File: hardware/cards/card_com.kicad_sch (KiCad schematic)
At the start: 18 parts, among them J1 DE9_Pins, J2 Conn_01x03, J3 Conn_01x04, U1 16550, U2 MAX3241, U3 74HCT04, U4 74HCT08, U5 74HCT08, U6 74HCT125

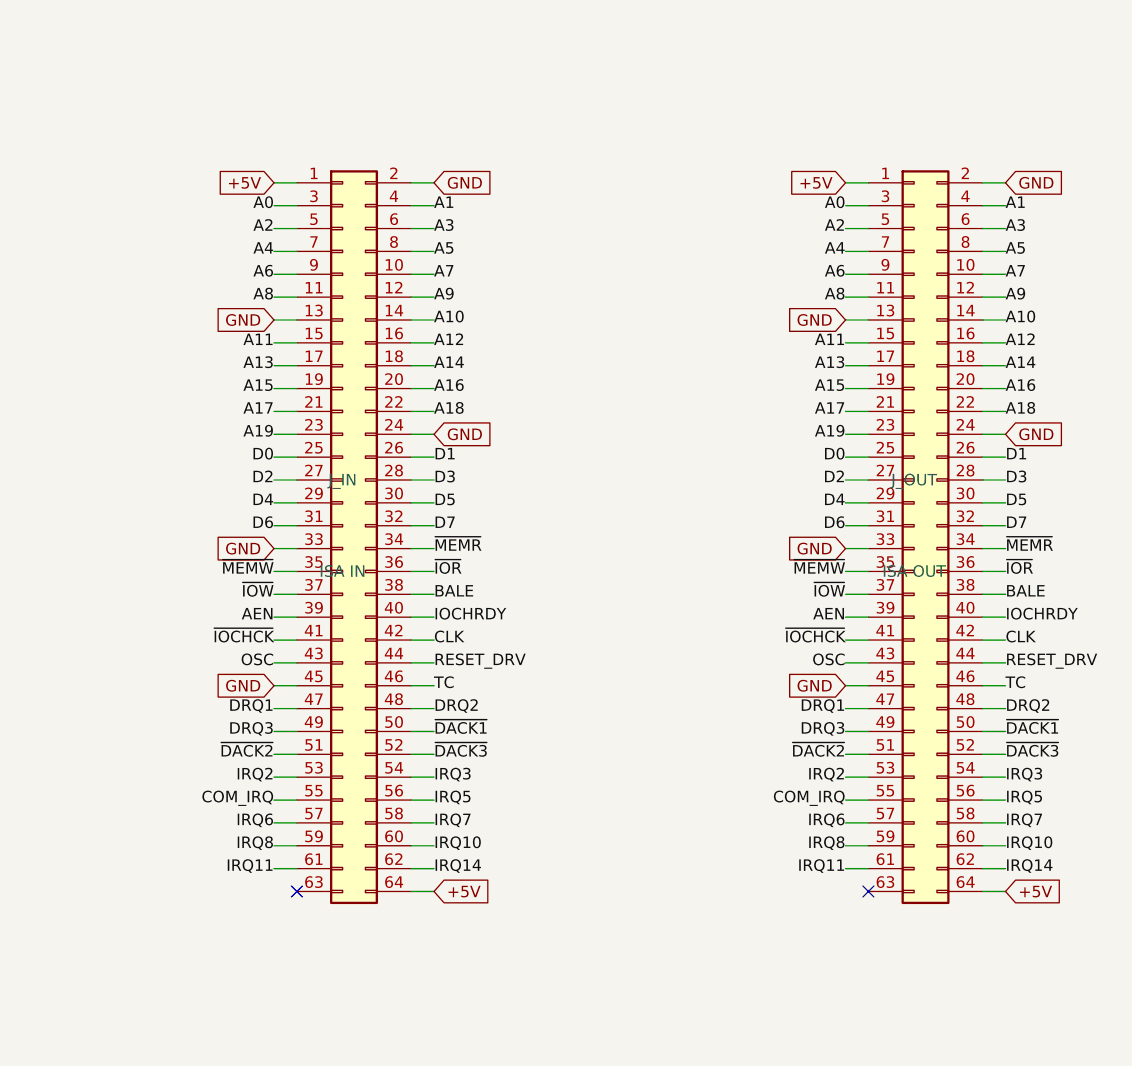
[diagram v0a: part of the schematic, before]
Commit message: Re-base ISA connector on standard 8-bit ISA pinout (60-pin, PicoGUS-style)
isa_conn now uses the standard 8-bit ISA edge pinout on a 60-pin 2.54mm header
(Conn_02x30_Odd_Even), matching the PicoGUS Bus_ISA_8bit layout so the sidecar and
dev cards are pin-compatible with real ISA cards (and 60-pin ribbon is easy to
source). The unused ISA analog rails are reclaimed: pin7 -5V->~{IOCHCK}, pin11
-12V->GND (extra return), pin15 +12V->IRQ8; pin13 reserved/0WS# left NC. Drops the
non-standard IRQ10/11/14 (16-bit-extension signals on a real AT); DACK0/REFRESH#
now on its standard pin (undriven, for card compatibility). Change is confined to
isa_conn.py; sidecar + all card_* sheets inherit it. Verified pin map and
connectivity (IOCHCK->Bus MCU, IRQ8->collector+RTC); zero structural ERC on
motherboard and all five cards.

Co-Authored-By: Claude Opus 4.8 (1M context) <noreply@anthropic.com>
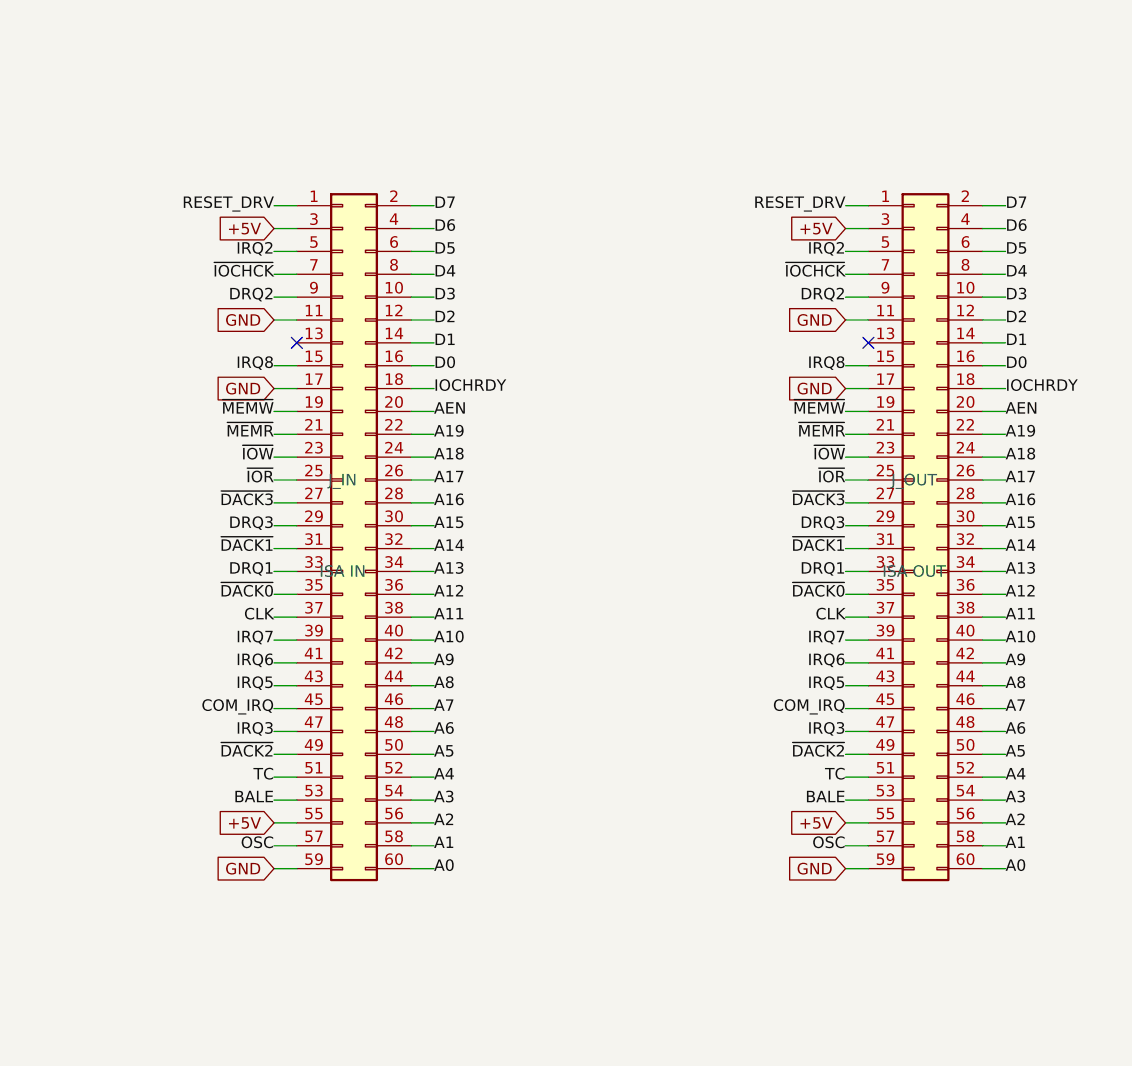
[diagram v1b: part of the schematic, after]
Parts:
- removed J_IN: ISA IN, symbol Connector_Generic:Conn_02x32_Odd_Even
- removed J_OUT: ISA OUT, symbol Connector_Generic:Conn_02x32_Odd_Even
- added J_IN: ISA IN, symbol Connector_Generic:Conn_02x30_Odd_Even
- added J_OUT: ISA OUT, symbol Connector_Generic:Conn_02x30_Odd_Even
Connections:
- net +5V: now also J_IN.3 (Pin_3), J_IN.55 (Pin_55), J_OUT.3 (Pin_3), J_OUT.55 (Pin_55)
- net A0: now also J_IN.60 (Pin_60), J_OUT.60 (Pin_60)
- net A1: now also J_IN.58 (Pin_58), J_OUT.58 (Pin_58)
- net A10: now also J_IN.40 (Pin_40), J_OUT.40 (Pin_40)
- net A11: now also J_IN.38 (Pin_38), J_OUT.38 (Pin_38)
- net A12: now also J_IN.36 (Pin_36), J_OUT.36 (Pin_36)
- net A13: now also J_IN.34 (Pin_34), J_OUT.34 (Pin_34)
- net A14: now also J_IN.32 (Pin_32), J_OUT.32 (Pin_32)
- net A15: now also J_IN.30 (Pin_30), J_OUT.30 (Pin_30)
- net A16: now also J_IN.28 (Pin_28), J_OUT.28 (Pin_28)
- net A17: now also J_IN.26 (Pin_26), J_OUT.26 (Pin_26)
- net A18: now also J_IN.24 (Pin_24), J_OUT.24 (Pin_24)
- net A19: now also J_IN.22 (Pin_22), J_OUT.22 (Pin_22)
- net A2: now also J_IN.56 (Pin_56), J_OUT.56 (Pin_56)
- net A3: now also J_IN.54 (Pin_54), J_OUT.54 (Pin_54)
- net A4: now also J_IN.52 (Pin_52), J_OUT.52 (Pin_52)
- net A5: now also J_IN.50 (Pin_50), J_OUT.50 (Pin_50)
- net A6: now also J_IN.48 (Pin_48), J_OUT.48 (Pin_48)
- net A7: now also J_IN.46 (Pin_46), J_OUT.46 (Pin_46)
- net A8: now also J_IN.44 (Pin_44), J_OUT.44 (Pin_44)
- net A9: now also J_IN.42 (Pin_42), J_OUT.42 (Pin_42)
- net AEN: now also J_IN.20 (Pin_20), J_OUT.20 (Pin_20)
- net BALE: now also J_IN.53 (Pin_53), J_OUT.53 (Pin_53)
- net CLK: now also J_IN.37 (Pin_37), J_OUT.37 (Pin_37)
- net COM_IRQ: now also J_IN.45 (Pin_45), J_OUT.45 (Pin_45)
- net D0: now also J_IN.16 (Pin_16), J_OUT.16 (Pin_16)
- net D1: now also J_IN.14 (Pin_14), J_OUT.14 (Pin_14)
- net D2: now also J_IN.12 (Pin_12), J_OUT.12 (Pin_12)
- net D3: now also J_IN.10 (Pin_10), J_OUT.10 (Pin_10)
- net D4: now also J_IN.8 (Pin_8), J_OUT.8 (Pin_8)
- net D5: now also J_IN.6 (Pin_6), J_OUT.6 (Pin_6)
- net D6: now also J_IN.4 (Pin_4), J_OUT.4 (Pin_4)
- net D7: now also J_IN.2 (Pin_2), J_OUT.2 (Pin_2)
- net DRQ1: now also J_IN.33 (Pin_33), J_OUT.33 (Pin_33)
- net DRQ2: now also J_IN.9 (Pin_9), J_OUT.9 (Pin_9)
- net DRQ3: now also J_IN.29 (Pin_29), J_OUT.29 (Pin_29)
- net GND: now also J_IN.11 (Pin_11), J_IN.17 (Pin_17), J_IN.59 (Pin_59), J_OUT.11 (Pin_11), J_OUT.17 (Pin_17), J_OUT.59 (Pin_59)
- net IOCHRDY: now also J_IN.18 (Pin_18), J_OUT.18 (Pin_18)
- net IRQ2: now also J_IN.5 (Pin_5), J_OUT.5 (Pin_5)
- net IRQ3: now also J_IN.47 (Pin_47), J_OUT.47 (Pin_47)
- net IRQ5: now also J_IN.43 (Pin_43), J_OUT.43 (Pin_43)
- net IRQ6: now also J_IN.41 (Pin_41), J_OUT.41 (Pin_41)
- net IRQ7: now also J_IN.39 (Pin_39), J_OUT.39 (Pin_39)
- net IRQ8: now also J_IN.15 (Pin_15), J_OUT.15 (Pin_15)
- net OSC: now also J_IN.57 (Pin_57), J_OUT.57 (Pin_57)
- net RESET_DRV: now also J_IN.1 (Pin_1), J_OUT.1 (Pin_1)
- net TC: now also J_IN.51 (Pin_51), J_OUT.51 (Pin_51)
- net ~{DACK1}: now also J_IN.31 (Pin_31), J_OUT.31 (Pin_31)
- net ~{DACK2}: now also J_IN.49 (Pin_49), J_OUT.49 (Pin_49)
- net ~{DACK3}: now also J_IN.27 (Pin_27), J_OUT.27 (Pin_27)
- net ~{IOCHCK}: now also J_IN.7 (Pin_7), J_OUT.7 (Pin_7)
- net ~{IOR}: now also J_IN.25 (Pin_25), J_OUT.25 (Pin_25)
- net ~{IOW}: now also J_IN.23 (Pin_23), J_OUT.23 (Pin_23)
- net ~{MEMR}: now also J_IN.21 (Pin_21), J_OUT.21 (Pin_21)
- net ~{MEMW}: now also J_IN.19 (Pin_19), J_OUT.19 (Pin_19)
- new net ~{DACK0}: J_IN.35 (Pin_35), J_OUT.35 (Pin_35)

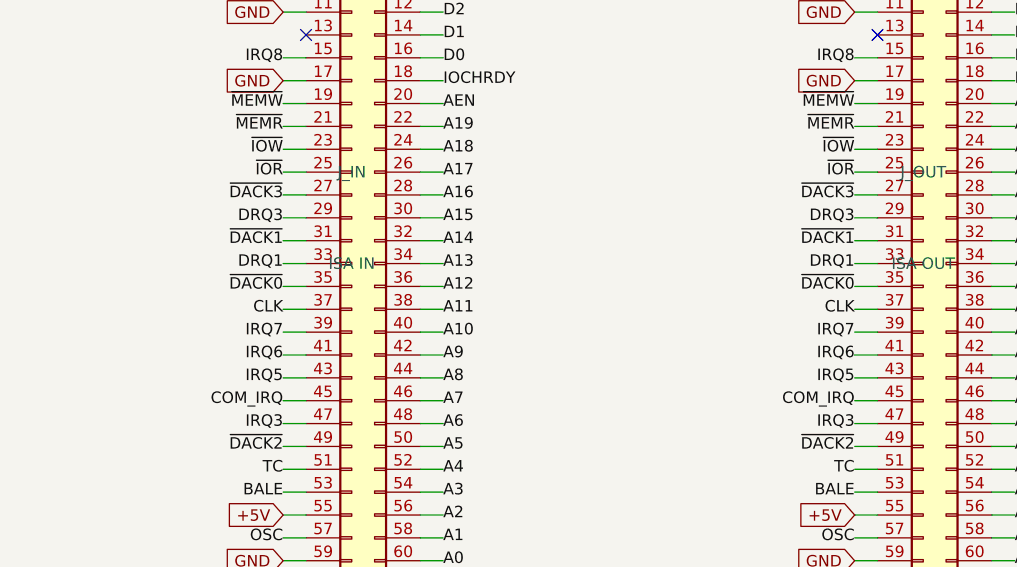
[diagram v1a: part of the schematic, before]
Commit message: Drive ISA REFRESH# from the Bus MCU for DRAM-based cards
Pin 35 (DACK0/REFRESH#) net renamed ~{DACK0} -> ~{REFRESH} in isa_conn and is now
an active Bus MCU output (GPIO47, reclaimed from the redundant raw-~WR sense -- the
MCU tracks writes via the gated MEMW/IOW). Driven from the internal ~15us refresh
timer (same source as the 0x61-bit-4 toggle); a refresh cycle reuses the bus-master
engine to walk the row address on A0-A7 + pulse MEMR#, so DRAM ISA cards see a
standard refresh. ~{REFRESH} added to the Bus MCU interface. Verified it ties
sidecar<->Bus MCU and passes through J_IN<->J_OUT on every dev card; zero
structural ERC on motherboard and all five cards.

Co-Authored-By: Claude Opus 4.8 (1M context) <noreply@anthropic.com>
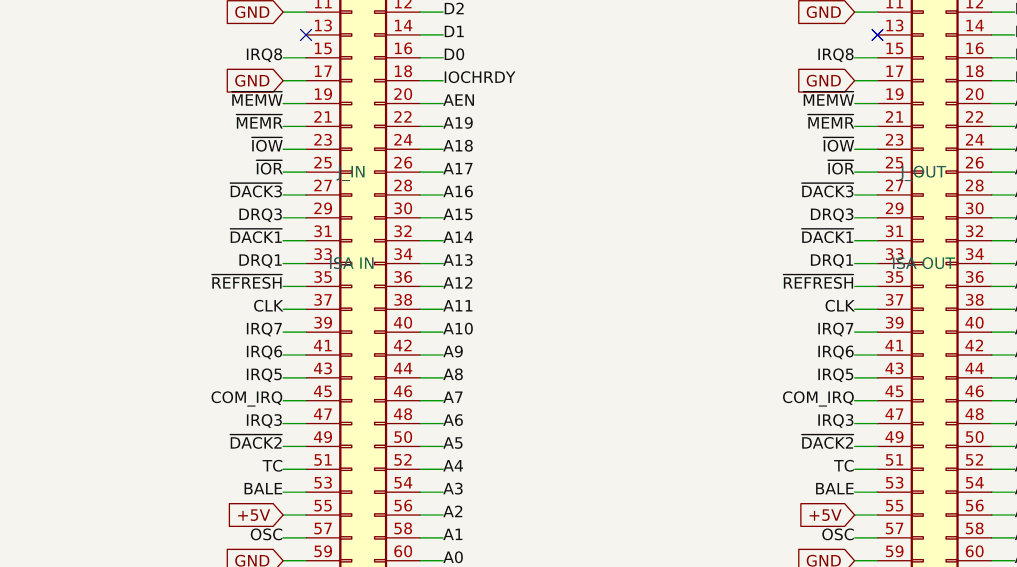
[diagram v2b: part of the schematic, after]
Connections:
- net ~{DACK0} renamed ~{REFRESH}
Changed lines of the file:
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@@
 		)
 	)
-	(label "~{DACK0}"
+	(label "~{REFRESH}"
 		(at 436.88 160.02 180)
 		(effects
@@
 		)
 	)
-	(label "~{DACK0}"
+	(label "~{REFRESH}"
 		(at 500.38 160.02 180)
 		(effects
@@
 		(instances
 			(project "card_com"
-				(path "/16270df2-9933-4f75-ad06-9b0b426deaac"
+				(path "/8767b612-b64f-46fa-82a4-7980ede15a86"
 					(reference "J_IN")
 					(unit 1)
@@
 		(instances
 			(project "card_com"
-				(path "/16270df2-9933-4f75-ad06-9b0b426deaac"
+				(path "/8767b612-b64f-46fa-82a4-7980ede15a86"
 					(reference "J_OUT")
 					(unit 1)
@@
 		(instances
 			(project "card_com"
-				(path "/16270df2-9933-4f75-ad06-9b0b426deaac"
+				(path "/8767b612-b64f-46fa-82a4-7980ede15a86"
 					(reference "U1")
 					(unit 1)
@@
 		(instances
 			(project "card_com"
-				(path "/16270df2-9933-4f75-ad06-9b0b426deaac"
+				(path "/8767b612-b64f-46fa-82a4-7980ede15a86"
 					(reference "OSC1")
 					(unit 1)
@@
 		(instances
 			(project "card_com"
-				(path "/16270df2-9933-4f75-ad06-9b0b426deaac"
+				(path "/8767b612-b64f-46fa-82a4-7980ede15a86"
 					(reference "U3")
 					(unit 1)
@@
 		(instances
 			(project "card_com"
-				(path "/16270df2-9933-4f75-ad06-9b0b426deaac"
+				(path "/8767b612-b64f-46fa-82a4-7980ede15a86"
 					(reference "J2")
 					(unit 1)
@@
 		(instances
 			(project "card_com"
-				(path "/16270df2-9933-4f75-ad06-9b0b426deaac"
+				(path "/8767b612-b64f-46fa-82a4-7980ede15a86"
 					(reference "U4")
 					(unit 1)
@@
 		(instances
 			(project "card_com"
-				(path "/16270df2-9933-4f75-ad06-9b0b426deaac"
+				(path "/8767b612-b64f-46fa-82a4-7980ede15a86"
 					(reference "U5")
 					(unit 1)
@@
 		(instances
 			(project "card_com"
-				(path "/16270df2-9933-4f75-ad06-9b0b426deaac"
+				(path "/8767b612-b64f-46fa-82a4-7980ede15a86"
 					(reference "U6")
 					(unit 1)
@@
 		(instances
 			(project "card_com"
-				(path "/16270df2-9933-4f75-ad06-9b0b426deaac"
+				(path "/8767b612-b64f-46fa-82a4-7980ede15a86"
 					(reference "U2")
 					(unit 1)
@@
 		(instances
 			(project "card_com"
-				(path "/16270df2-9933-4f75-ad06-9b0b426deaac"
+				(path "/8767b612-b64f-46fa-82a4-7980ede15a86"
 					(reference "C3")
 					(unit 1)
@@
 		(instances
 			(project "card_com"
-				(path "/16270df2-9933-4f75-ad06-9b0b426deaac"
+				(path "/8767b612-b64f-46fa-82a4-7980ede15a86"
 					(reference "C4")
 					(unit 1)
@@
 		(instances
 			(project "card_com"
-				(path "/16270df2-9933-4f75-ad06-9b0b426deaac"
+				(path "/8767b612-b64f-46fa-82a4-7980ede15a86"
 					(reference "C5")
 					(unit 1)
@@
 		(instances
 			(project "card_com"
-				(path "/16270df2-9933-4f75-ad06-9b0b426deaac"
+				(path "/8767b612-b64f-46fa-82a4-7980ede15a86"
 					(reference "C6")
 					(unit 1)
@@
 		(instances
 			(project "card_com"
-				(path "/16270df2-9933-4f75-ad06-9b0b426deaac"
+				(path "/8767b612-b64f-46fa-82a4-7980ede15a86"
 					(reference "J1")
 					(unit 1)
@@
 		(instances
 			(project "card_com"
-				(path "/16270df2-9933-4f75-ad06-9b0b426deaac"
+				(path "/8767b612-b64f-46fa-82a4-7980ede15a86"
 					(reference "J3")
 					(unit 1)
@@
 		(instances
 			(project "card_com"
-				(path "/16270df2-9933-4f75-ad06-9b0b426deaac"
+				(path "/8767b612-b64f-46fa-82a4-7980ede15a86"
 					(reference "C1")
 					(unit 1)
@@
 		(instances
 			(project "card_com"
-				(path "/16270df2-9933-4f75-ad06-9b0b426deaac"
+				(path "/8767b612-b64f-46fa-82a4-7980ede15a86"
 					(reference "C2")
 					(unit 1)
